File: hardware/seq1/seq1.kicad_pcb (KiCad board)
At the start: 2 copper layers, 190.5 x 141.5 mm, 159 parts, among them J1 AudioJack2_SwitchT, J10 Conn_01x04, J11 Conn_01x04, J12 Conn_01x04, J13 Conn_01x04, J14 Conn_01x04, J15 Conn_01x04, J16 Conn_01x04, J17 Conn_01x04, J18 Conn_01x04, J19 Conn_01x04, J2 AudioJack2_SwitchT, J20 Conn_01x04, J21 Conn_01x04, J22 Conn_01x04, J23 Conn_01x04, J24 Conn_01x04, J25 Conn_01x04, J26 Conn_01x04, J27 Conn_01x04, J28 Conn_01x04, J3 Conn_02x08_Odd_Even, J4 AudioJack2_SwitchT, J5 AudioJack2_SwitchT, J6 Conn_01x04, J7 Conn_01x02, J8 AudioJack2_SwitchT, J9 AudioJack2_SwitchT, Q1 2N3904, SW1 SW_Push_x4, SW2 SW_Push_x4, SW3 SW_Push_x4, SW4 SW_Push_x4, SW5 SW_Push_x2, SW9 PEC12R-3220F-S0024, U10 TL072, U2 74HC4051, U3 74HC4051, U5 128x64 0.96" OLED I2C, U6 TL074, U7 TLV1117-33, U8 74HC4051, U9 74HC4051

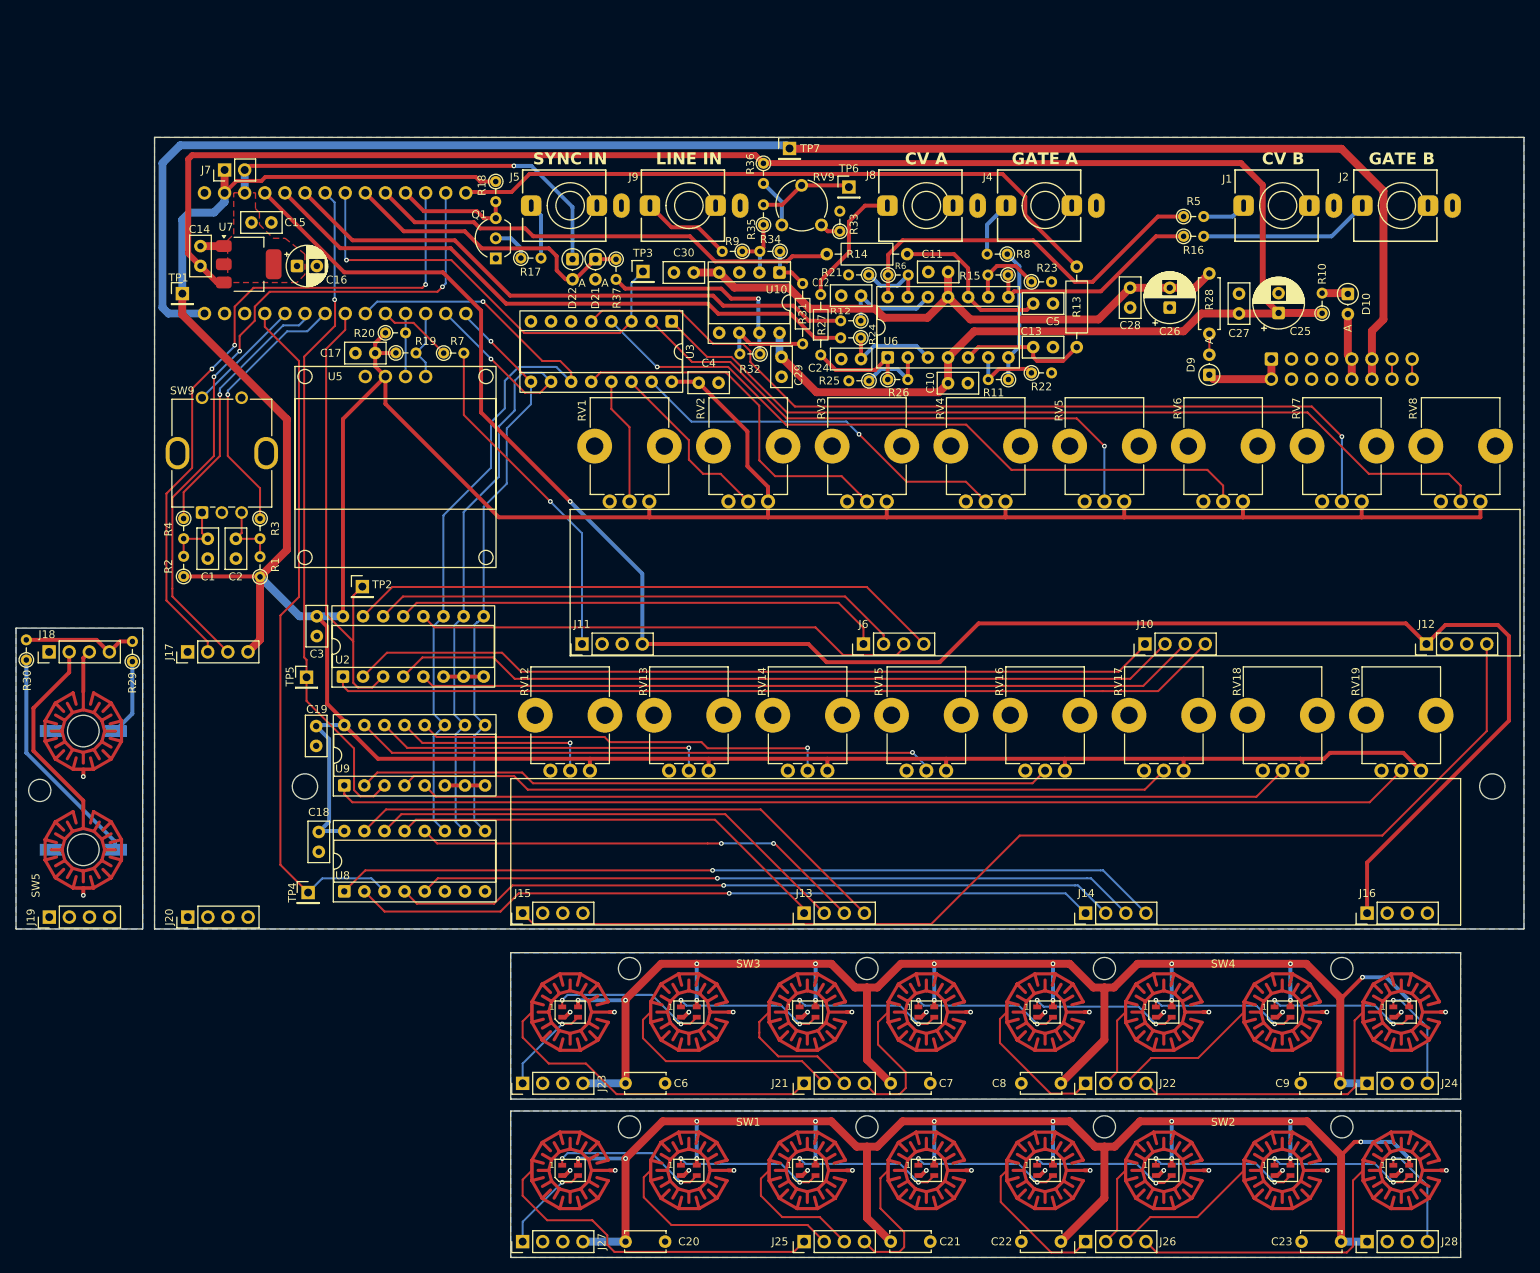
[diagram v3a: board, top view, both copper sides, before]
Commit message: moved 1x4 keypad to separate project
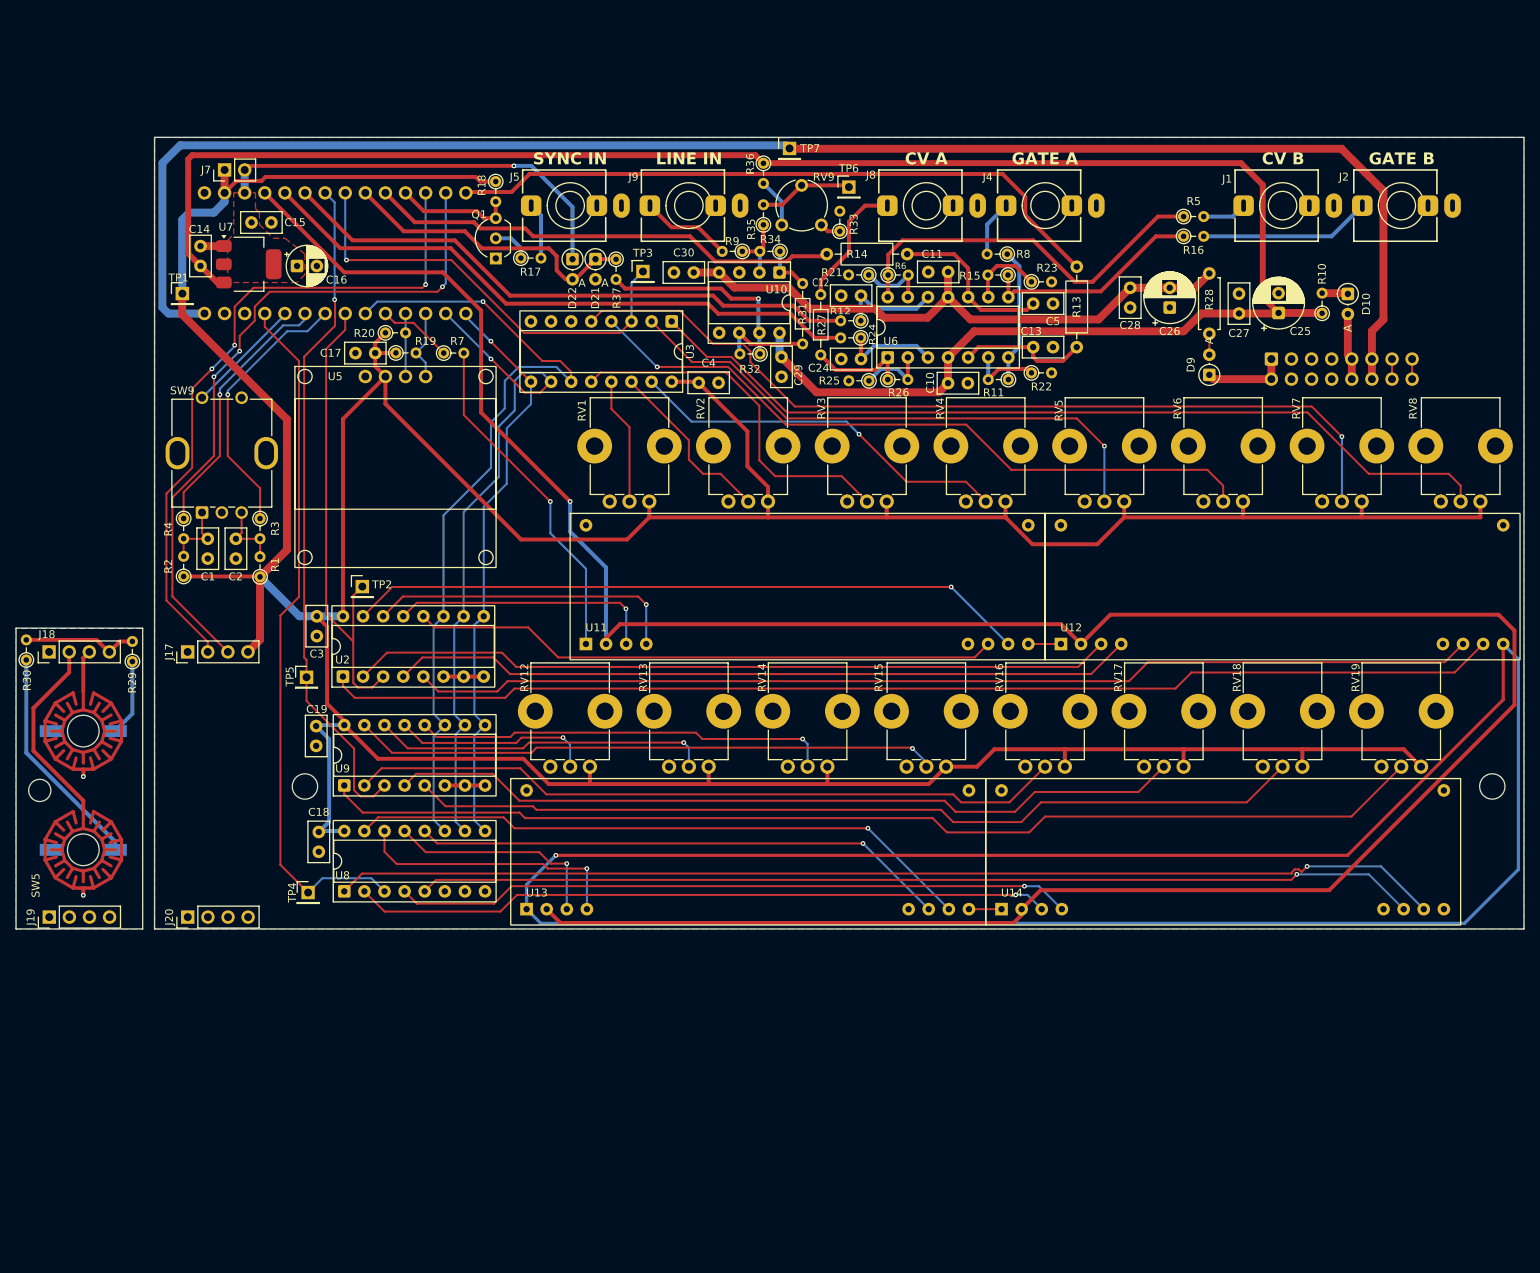
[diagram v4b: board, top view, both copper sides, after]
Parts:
- removed C20, C21, C22, C23, C6, C7, C8, C9: 1u, Capacitor_THT:C_Disc_D5.0mm_W2.5mm_P5.00mm
- removed D1, D11, D12, D13, D14, D15, D16, D17, D18, D2, D3, D4, D5, D6, D7, D8: SK6805, LED_SMD:LED_SK6805_PLCC4_2.4x2.7mm_P1.3mm
- removed J10, J11, J12, J13, J14, J15, J16, J21, J22, J23, J24, J25, J26, J27, J28, J6: Conn_01x04, Connector_PinHeader_2.54mm:PinHeader_1x04_P2.54mm_Vertical
- removed SW1, SW2, SW3, SW4: SW_Push_x4, Adafruit_Trellis:SW_Silicone_Keypad_PushButton_10mm_4x1grid_NH
- added U11: Neopixel Keypad 1x4, Adafruit_Trellis:SW_Keypad_PushButton_1x4_Riser, F.Cu at (97.5, 101.0)
- added U12: Neopixel Keypad 1x4, Adafruit_Trellis:SW_Keypad_PushButton_1x4_Riser, F.Cu at (157.5, 101.0)
- added U13: Neopixel Keypad 1x4, Adafruit_Trellis:SW_Keypad_PushButton_1x4_Riser, F.Cu at (90.0, 134.5)
- added U14: Neopixel Keypad 1x4, Adafruit_Trellis:SW_Keypad_PushButton_1x4_Riser, F.Cu at (150.0, 134.5)
- moved RV12 0.50 mm to (100.0, 114.5)
- moved RV13 0.50 mm to (115.0, 114.5)
- moved RV14 0.50 mm to (130.0, 114.5)
- moved RV15 0.50 mm to (145.0, 114.5)
- moved RV16 0.50 mm to (160.0, 114.5)
- moved RV17 0.50 mm to (175.0, 114.5)
- moved RV18 0.50 mm to (190.0, 114.5)
- moved RV19 0.50 mm to (205.0, 114.5)
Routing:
- net Net-(U12-DOUT): track 0.00 -> 301.3 mm, vias 0 -> 1
- net /neopxls/+5V_SB3: track 208.2 -> 0.00 mm, vias 16 -> 0
- net /neopxls/+5V_SB2: track 208.2 -> 0.00 mm, vias 16 -> 0
- net /neopxls/DOUT_NPXL_1: track 143.5 -> 0.00 mm
- net +5V: track 241.6 -> 346.0 mm
- net Net-(J25-Pin_1): track 43.4 -> 0.00 mm
- net Net-(J21-Pin_1): track 42.8 -> 0.00 mm
- net Net-(J22-Pin_4): track 37.2 -> 0.00 mm
- net Net-(J26-Pin_4): track 37.2 -> 0.00 mm
- net Net-(U12-D3): track 112.9 -> 148.7 mm
- net Net-(U12-D2): track 98.9 -> 134.6 mm
- net Net-(U14-D3): track 104.6 -> 140.3 mm
- net Net-(U14-D2): track 91.7 -> 127.0 mm
- net Net-(U11-D0): track 62.7 -> 33.6 mm, vias 0 -> 1
- net Net-(J21-Pin_2): track 29.0 -> 0.00 mm
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- removed copper zone on B.Cu, net /neopxls/GND_SB2
- removed copper zone on B.Cu, net /neopxls/GND_SB3
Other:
- board size 190.5 x 141.5 mm -> 190.5 x 100 mm
- board text removed: "Split to 1x4, remove from project as separate board"

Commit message: updated schematic title blocks for v2, generated gerbers
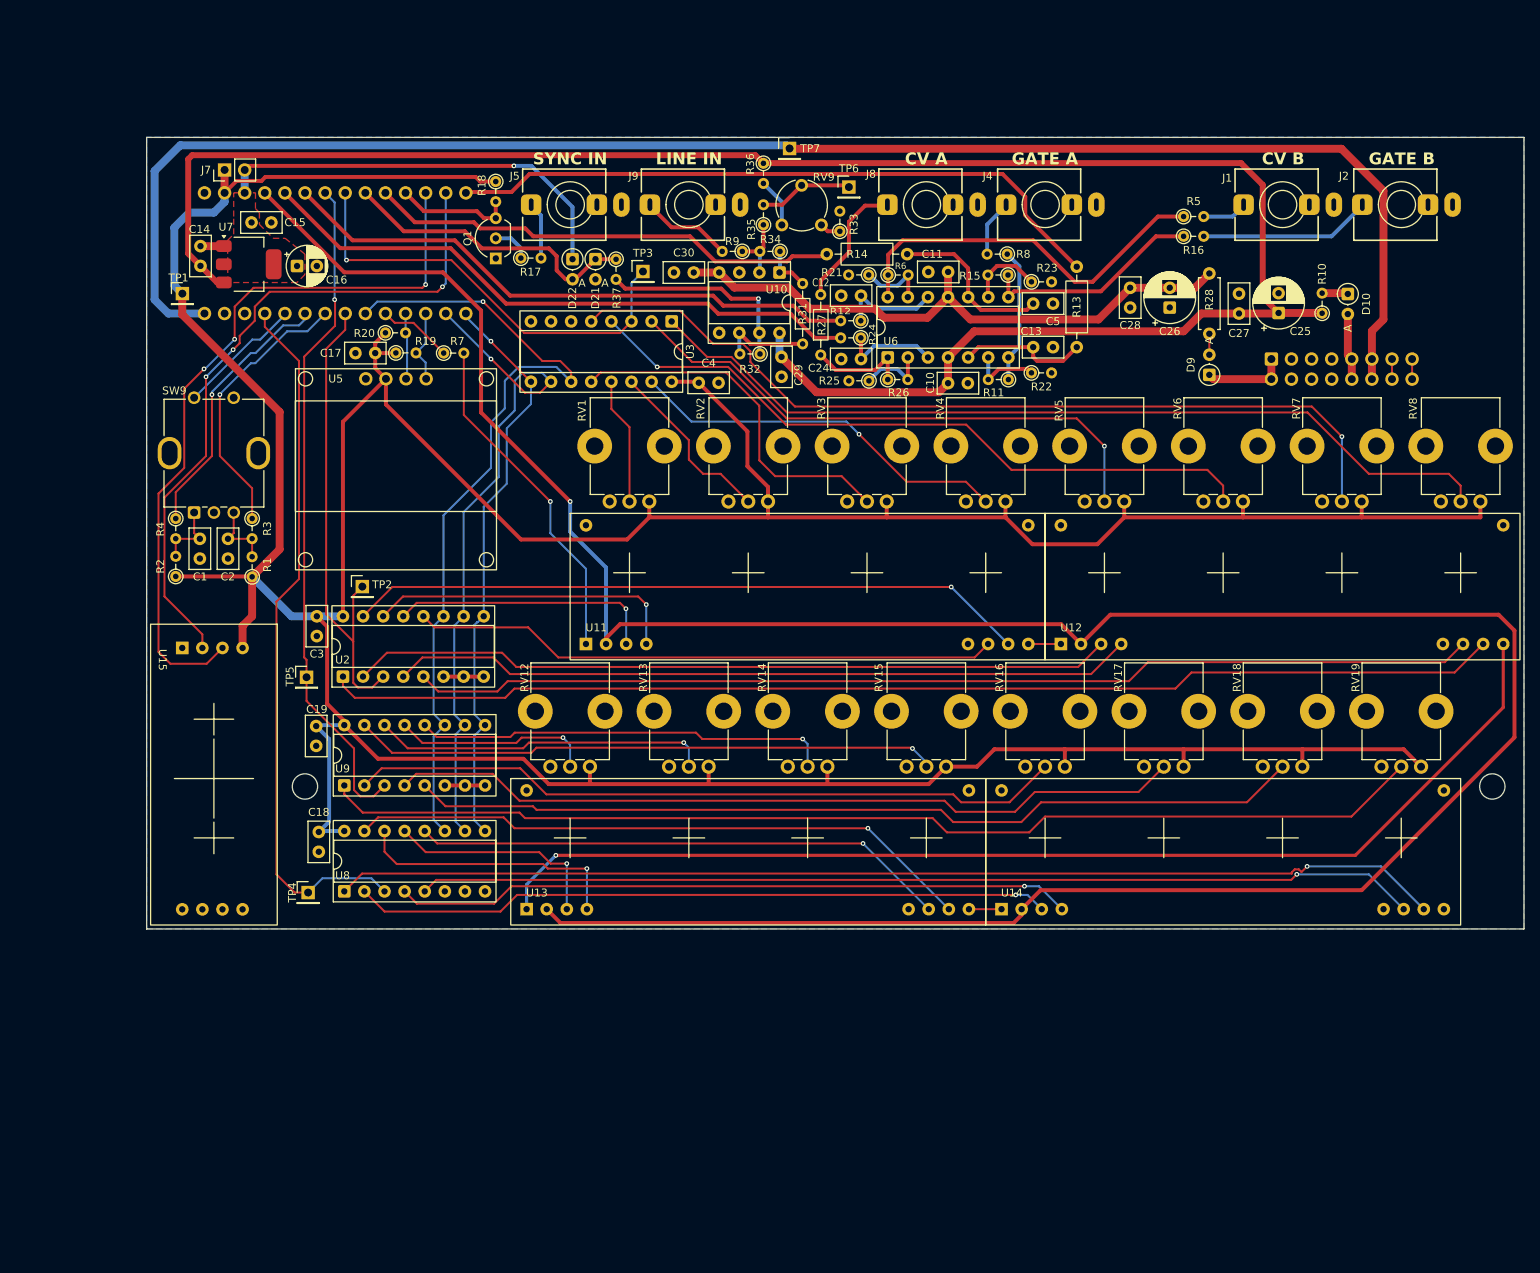
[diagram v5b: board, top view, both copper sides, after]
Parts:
- removed D19, D20: LED, Adafruit_Trellis:LED_3mm_Backside_SMD
- removed J17, J18, J19, J20: Conn_01x04, Connector_PinHeader_2.54mm:PinHeader_1x04_P2.54mm_Vertical
- removed R29, R30: 1.2k, Resistor_THT:R_Axial_DIN0204_L3.6mm_D1.6mm_P2.54mm_Vertical
- removed SW5: SW_Push_x2, Adafruit_Trellis:SW_Silicone_Keypad_PushButton_10mm_2x1grid_NH
- added U15: 1x2 LED Keypad, Adafruit_Trellis:SW_Keypad_PushButton_1x2_Riser, F.Cu at (44.5, 96.5)
- moved C1 1.00 mm to (50.7, 85.7)
- moved C2 1.00 mm to (54.3, 85.7)
- moved R1 1.00 mm to (57.3, 90.5)
- moved R2 1.00 mm to (47.7, 90.5)
- moved R3 1.00 mm to (57.3, 83.2)
- moved R4 1.00 mm to (47.7, 83.2)
- moved SW9 1.00 mm to (50.0, 82.4)
- moved U5 0.30 mm to (75.5, 76.9)
- moved J1 0.12 mm to (187.5, 43.5)
- moved J2 0.12 mm to (202.5, 43.5)
- moved J4 0.12 mm to (157.5, 43.5)
- moved J5 0.12 mm to (97.5, 43.5)
- moved J8 0.12 mm to (142.5, 43.5)
- moved J9 0.12 mm to (112.5, 43.5)
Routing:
- net Net-(U12-DOUT): track 301.3 -> 143.8 mm
- net Net-(D20-A): track 28.6 -> 0.00 mm
- net /mcu/N_RUN_SB1: track 24.5 -> 0.00 mm
- net /mcu/3V3_SB1: track 14.6 -> 0.00 mm
- net Net-(D19-A): track 9.39 -> 0.00 mm
- net /mcu/N_RUN: track 86.4 -> 94.3 mm
- net /mcu/N_MODE_SB1: track 5.31 -> 0.00 mm
- net +5V: track 346.0 -> 348.4 mm
- net /mcu/GND_SB1: track 1.85 -> 0.00 mm, vias 2 -> 0
- net SW_MUX_B: track 88.4 -> 89.8 mm
- net /mcu/N_MODE: track 87.6 -> 86.6 mm
- net /mcu/ROT_SW: track 15.0 -> 16.0 mm
- net +3V3: track 554.5 -> 555.5 mm
- net +5V_IN: track 205.8 -> 206.7 mm
- net /mcu/RSWB: track 33.4 -> 34.2 mm
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- removed copper zone on B.Cu, net /mcu/GND_SB1
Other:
- board size 190.5 x 100 mm -> 174 x 100 mm
- board text added: "v2.0.20251107 CC BY-SA 4.0 idyllm"
- board text removed: "v1.1.20241014 CC BY-SA 4.0 idyllm"
